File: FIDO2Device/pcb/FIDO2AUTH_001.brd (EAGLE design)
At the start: 22.9 x 38.7 mm, 33 parts, among them CN1 TE-1734028, CN2 IF_5PIN_H, CN3 IF_3PIN, SW1 SKRPACE010, SW2 SKTADAE010, U1 MDBT50Q-P1M, U2 XC6206P332MR-G, X1 NX3215SA-32.768K

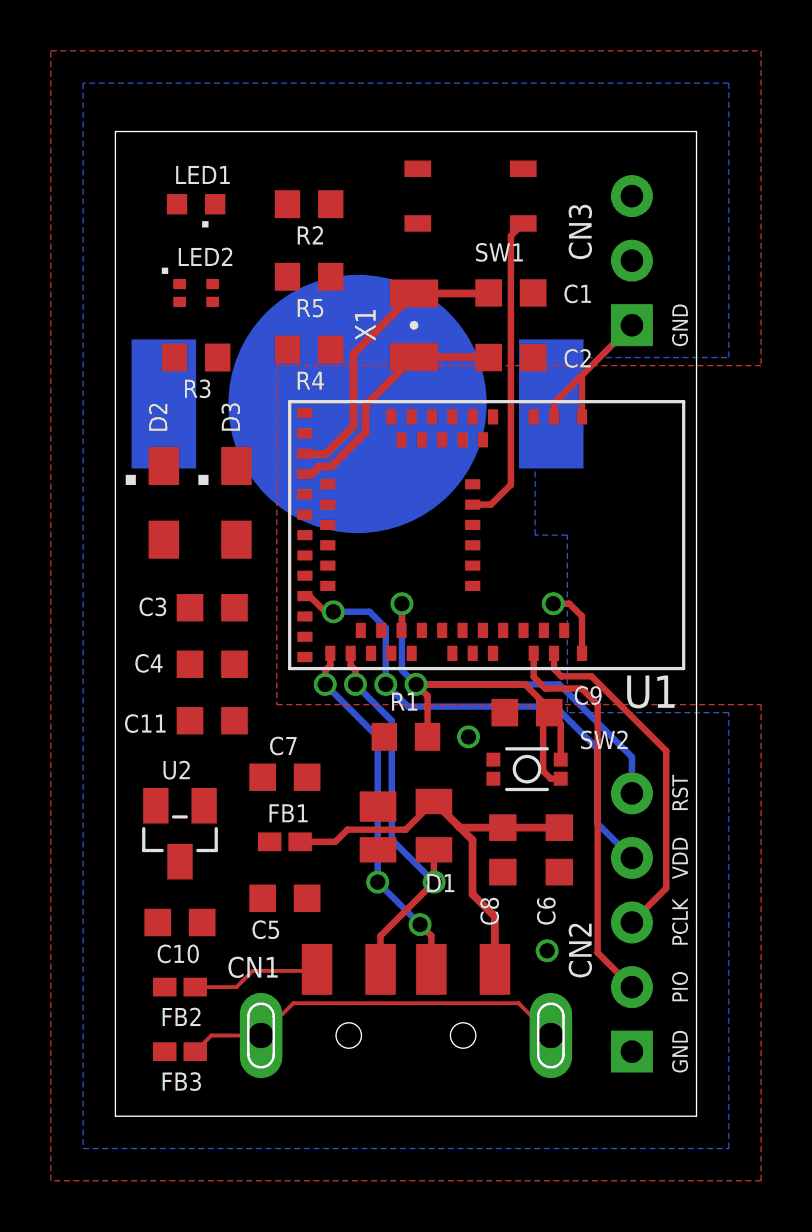
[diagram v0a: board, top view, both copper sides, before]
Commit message: ブレークアウト基板回路図
・汎用I/Oとして、デジタル／アナログ双方が使用できるピンを選定
・全ての配線を完了
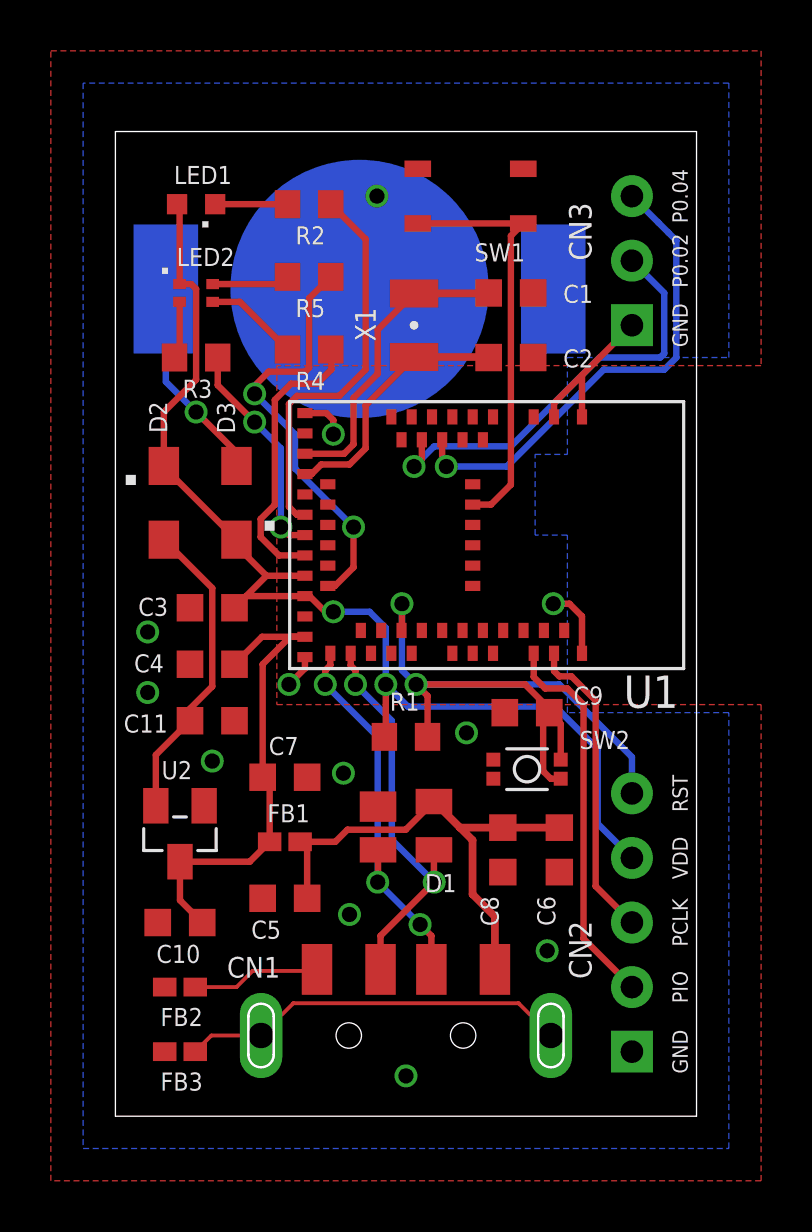
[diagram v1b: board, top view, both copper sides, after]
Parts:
- moved BAT1 4.53 mm to (9.60, 32.5)
- turned D3 to 90 degrees
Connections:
- new net AIN0: CN3.2, U1.11
- new net AIN1: CN3.3, U1.9
- net N$5: no longer BAT1.+@2
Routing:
- net VDD_NRF: track 20.2 -> 45.2 mm
- net VBUS_NRF: track 0.00 -> 19.0 mm
- net AIN1: track 0.00 -> 19.0 mm, vias 0 -> 1
- net AIN0: track 0.00 -> 17.0 mm, vias 0 -> 1
- net LED2_B: track 0.00 -> 16.4 mm, vias 0 -> 2
- net LED1: track 0.00 -> 15.5 mm
- net N$4: track 0.00 -> 12.2 mm
- net LED2_G: track 0.00 -> 11.2 mm
- net LED2_R: track 0.00 -> 8.77 mm, vias 0 -> 2
- net N$5: track 0.00 -> 8.11 mm, vias 0 -> 1
- net SW1: track 12.3 -> 16.5 mm
- net N$9: track 0.00 -> 3.72 mm
- net 0V: track 9.31 -> 12.4 mm, vias 3 -> 12
- net N$10: track 0.00 -> 3.06 mm
- net N$11: track 0.00 -> 2.84 mm
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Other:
- board text added: "P0.02"
- board text added: "P0.04"

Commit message: ブレークアウト基板回路図を修正
・３色LEDの配線が間違っていたので修正
・シルクの位置等を見直し
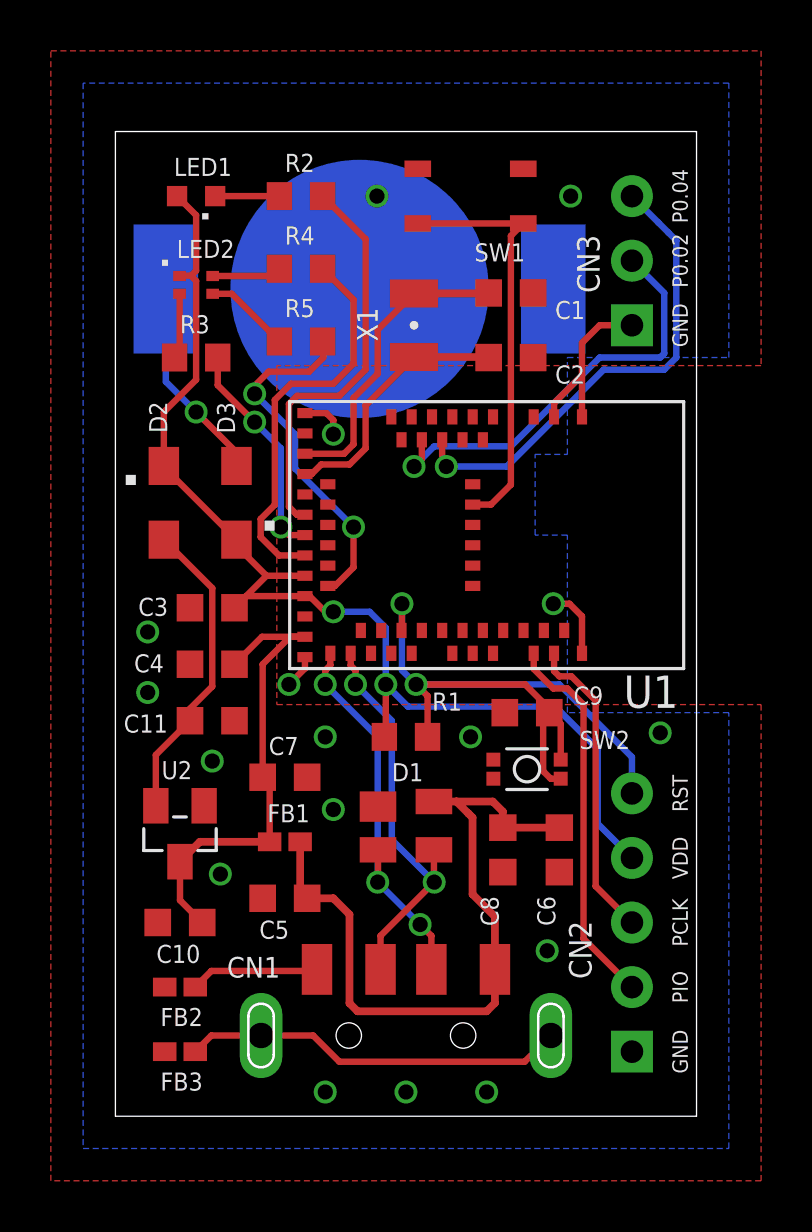
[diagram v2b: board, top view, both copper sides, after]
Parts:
- moved R4 3.19 mm to (7.30, 33.3)
- moved R5 2.56 mm to (7.30, 30.5)
- moved R2 0.45 mm to (7.30, 36.2)
- moved LED1 0.32 mm to (3.17, 36.2)
- moved LED2 0.32 mm to (3.17, 32.7)
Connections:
- removed net N$10: LED2.4, R5.2
- removed net N$9: LED2.3, R4.2
- new net N$6: LED2.4, R4.2
- new net N$7: LED2.3, R5.2
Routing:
- net VBUS: track 19.8 -> 28.1 mm
- net LED2_G: track 11.2 -> 15.6 mm
- net N$9: track 3.72 -> 0.00 mm
- net N$7: track 0.00 -> 3.40 mm
- net N$10: track 3.06 -> 0.00 mm
- net N$6: track 0.00 -> 2.75 mm
- net LED2_B: track 16.4 -> 13.9 mm
- net 0V: track 12.4 -> 13.2 mm, vias 12 -> 17
- net VDD_NRF: track 45.2 -> 45.9 mm
